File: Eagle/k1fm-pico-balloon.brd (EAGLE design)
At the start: 26.4 x 41.1 mm, 42 parts, among them J1 I2C, J2 ICSP, J3 SERIAL, J4 POWER, Q1 ASTX-H11-25.000MHZ-T, Q2 DMP2305U, Q3 DMP2305U, U1 ATMEGA328, U2 Si5351A-B-GT, U3 MCP1754X-XXXXX/C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

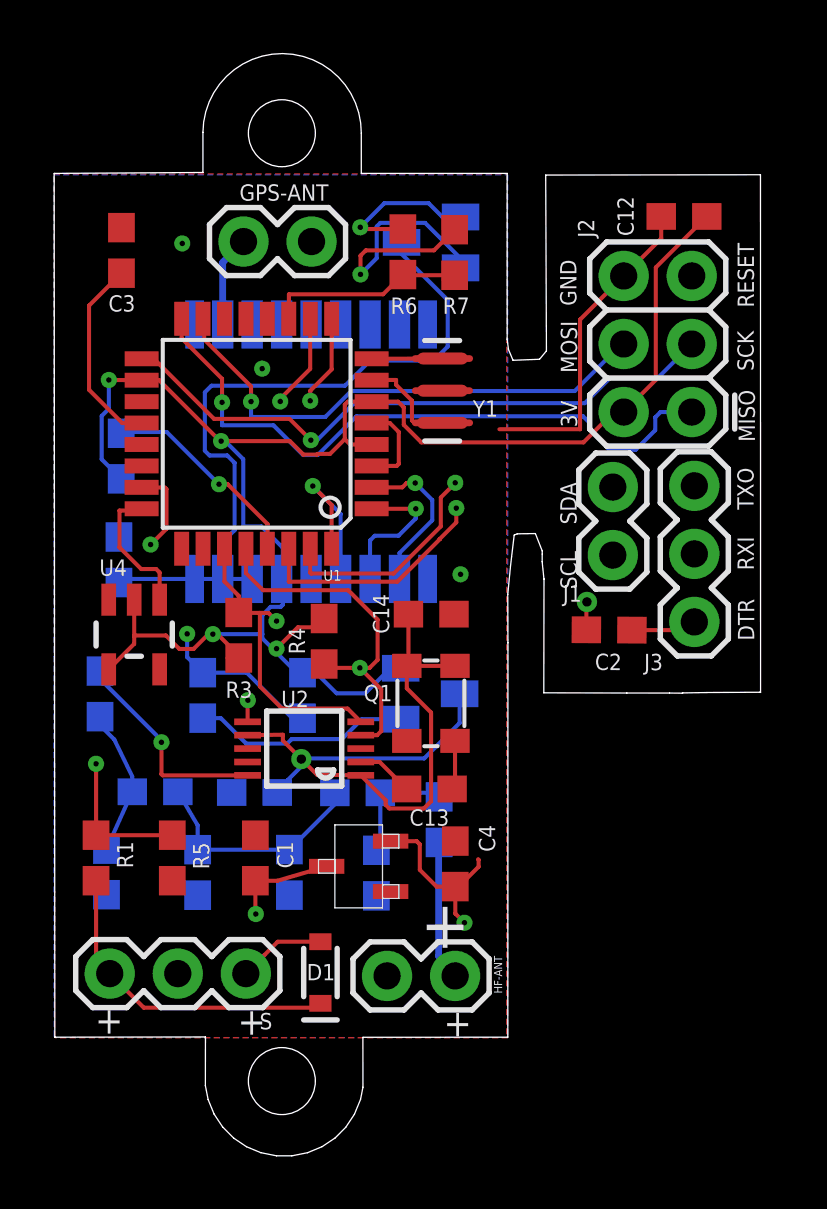
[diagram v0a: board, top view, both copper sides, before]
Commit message: Fix Mosfet polarization
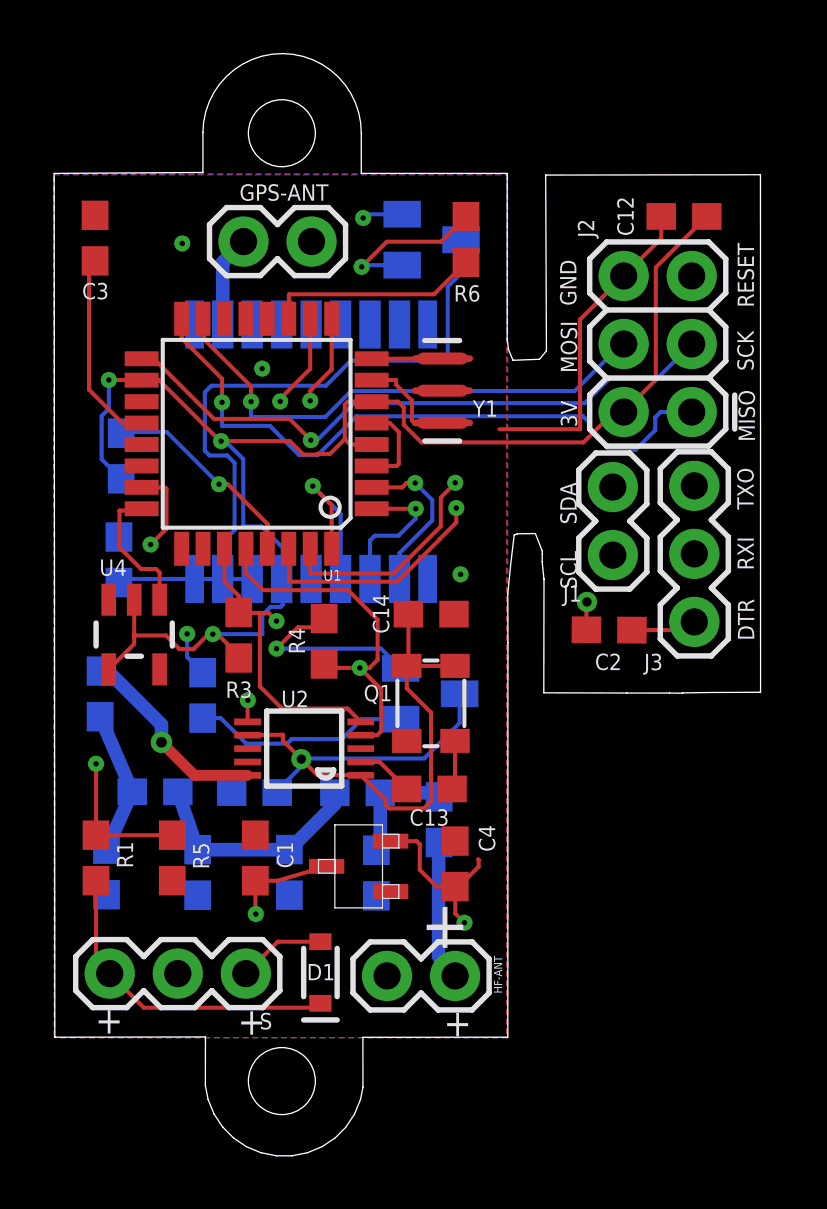
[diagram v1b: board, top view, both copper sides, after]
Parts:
- removed R7, R9: 10k, SparkFun-Resistors:0603
- R6, R8: value 150 -> 1K
- moved R6 2.40 mm to (14.4, 77.5)
- moved C3 1.09 mm to (0.53, 77.6)
- moved Q2 0.10 mm to (13.1, 77.5), turned to 90 degrees
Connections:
- net 3V: no longer R7.2, R9.2
- net GPS_E: no longer R7.1
- net TX_E: no longer R9.1
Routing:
- net 3V: track 110.6 -> 101.7 mm
- net TX_E: track 20.0 -> 15.6 mm
- net GPS_E: track 7.42 -> 8.06 mm
- net N$5: track 5.94 -> 6.49 mm
- net CLK0: track 8.03 -> 7.51 mm
- net N$12: track 6.36 -> 5.84 mm

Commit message: Expand gap
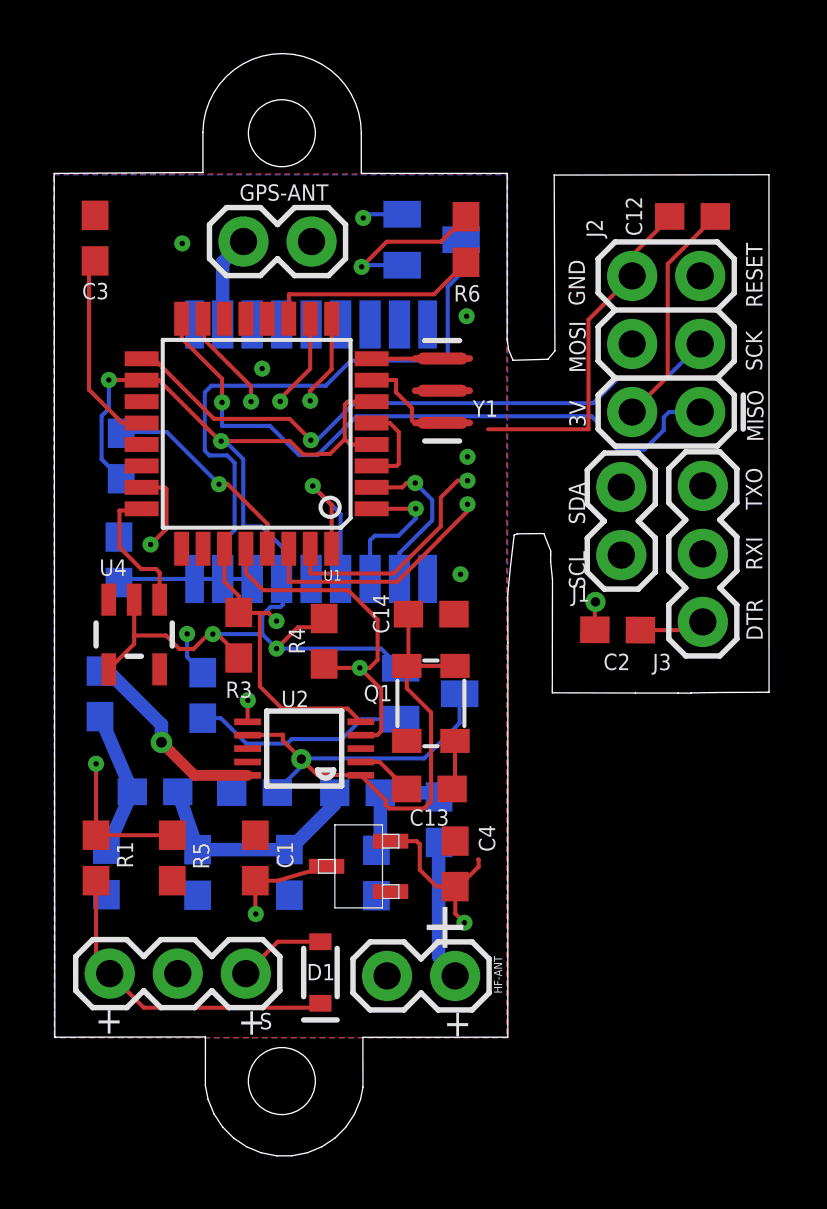
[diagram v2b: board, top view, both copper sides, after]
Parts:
- moved C12 0.32 mm to (22.8, 78.4)
- moved J2 0.32 mm to (23.1, 71.1)
- moved J3 0.32 mm to (23.2, 63.3)
- moved C2 0.32 mm to (20.0, 63.0)
- moved J1 0.32 mm to (20.2, 68.3)
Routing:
- net 3V: track 101.7 -> 108.0 mm
- net GND: track 15.6 -> 16.3 mm, vias 3 -> 5
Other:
- board size 26.4 x 41.1 mm -> 26.7 x 41.1 mm

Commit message: Fixed R1-R5 voltage divider, fixed PCB warnings
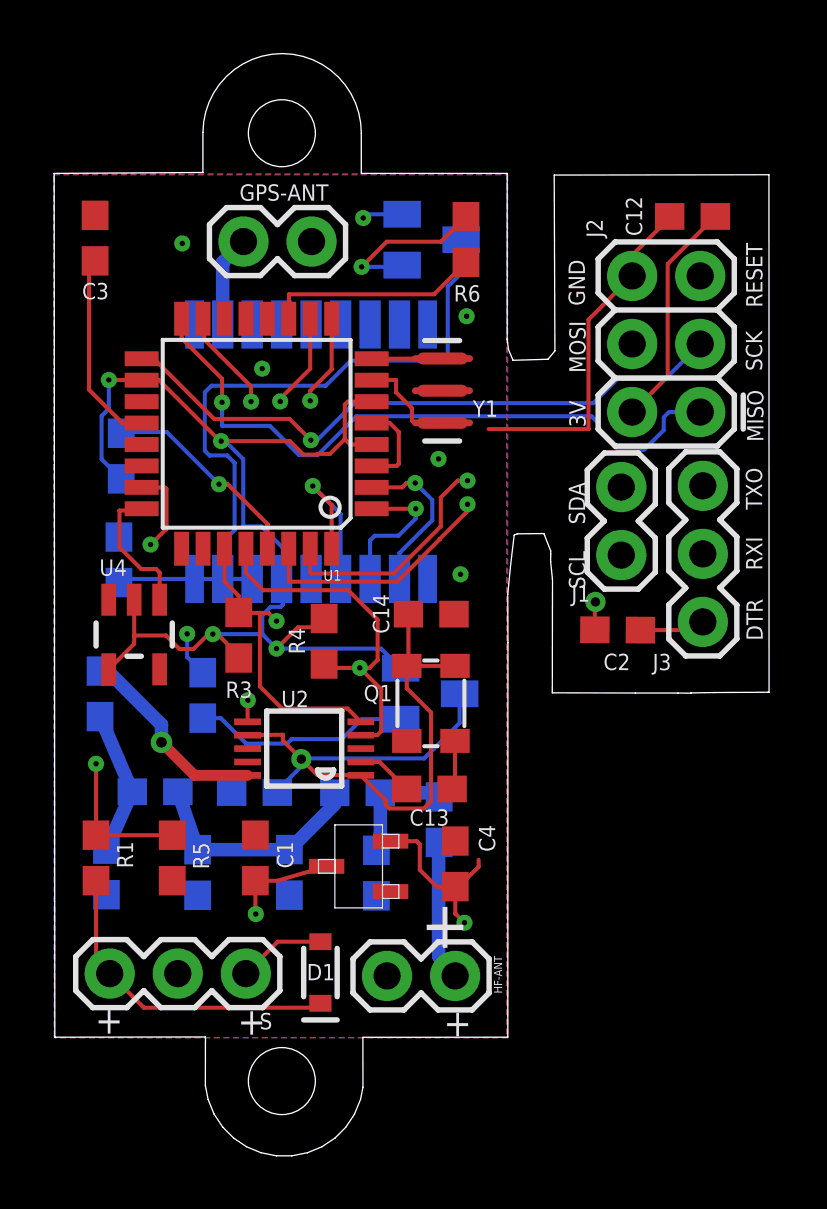
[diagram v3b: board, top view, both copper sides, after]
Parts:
- R5: value 4.7k -> 1k
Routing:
- net 3V: track 108.0 -> 106.5 mm
- net N$3: track 4.25 -> 3.28 mm
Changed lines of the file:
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@@
 <attribute name="VALUE" x="1.32644375" y="54.44650625" size="0.6096" layer="27" font="vector" ratio="20" rot="R90" align="top-center"/>
 </element>
-<element name="R5" library="SparkFun-Resistors" library_urn="urn:adsk.eagle:library:532" package="0603" package3d_urn="urn:adsk.eagle:package:39650/1" value="4.7k" x="3.40955" y="54.446978125" smashed="yes" rot="R90">
+<element name="R5" library="SparkFun-Resistors" library_urn="urn:adsk.eagle:library:532" package="0603" package3d_urn="urn:adsk.eagle:package:39650/1" value="1k" x="3.40955" y="54.446978125" smashed="yes" rot="R90">
 <attribute name="NAME" x="4.78984375" y="54.52568125" size="0.6096" layer="25" font="vector" ratio="20" rot="R90" align="bottom-center"/>
 <attribute name="PROD_ID" value="RES-00824" x="3.40955" y="54.446978125" size="1.27" layer="27" rot="R90" display="off"/>
@@
 <wire x1="20.5768875" y1="76.942765625" x2="20.5768875" y2="76.1720125" width="0.1524" layer="1"/>
 <wire x1="20.5768875" y1="76.1720125" x2="18.947928125" y2="74.543053125" width="0.1524" layer="1"/>
-<wire x1="18.947928125" y1="74.543053125" x2="18.947928125" y2="70.44936875" width="0.1524" layer="1"/>
+<wire x1="18.947928125" y1="74.543053125" x2="18.947928125" y2="70.45523125" width="0.1524" layer="1"/>
 <wire x1="10.850665625" y1="70.68035625" x2="11.53163125" y2="70.68035625" width="0.1524" layer="1"/>
 <wire x1="11.53163125" y1="70.68035625" x2="11.86534375" y2="70.34664375" width="0.1524" layer="1"/>
@@
 <via x="3.781075" y="77.385203125" extent="1-16" drill="0.2"/>
 <via x="14.3971125" y="74.66815" extent="1-16" drill="0.2"/>
-<via x="14.429625" y="69.4192" extent="1-16" drill="0.2"/>
-<wire x1="18.947928125" y1="70.44936875" x2="15.198228125" y2="70.44936875" width="0.1524" layer="1"/>
+<via x="13.348934375" y="69.3406125" extent="1-16" drill="0.2"/>
+<wire x1="18.947928125" y1="70.45523125" x2="15.21810625" y2="70.45523125" width="0.1524" layer="1"/>
 </signal>
 <signal name="3V">
@@
 <contactref element="U4" pad="4"/>
 <contactref element="GPS1" pad="6_V_BCKP"/>
-<wire x1="1.036578125" y1="61.486290625" x2="1.095696875" y2="61.486290625" width="0.1524" layer="1"/>
 <wire x1="1.98658125" y1="64.0864875" x2="1.986578125" y2="64.086490625" width="0.1524" layer="1"/>
-<wire x1="1.036578125" y1="61.358659375" x2="1.036578125" y2="61.486290625" width="0.1524" layer="1"/>
-<wire x1="7.379503125" y1="64.749571875" x2="7.49139375" y2="64.8614625" width="0.1524" layer="16"/>
 <contactref element="Q3" pad="2"/>
 <wire x1="2.265465625" y1="72.28035625" x2="1.041303125" y2="72.288534375" width="0.1524" layer="1"/>
 <via x="1.041303125" y="72.288534375" extent="1-16" drill="0.2"/>
-<wire x1="11.538078125" y1="55.050225" x2="11.56031875" y2="55.072465625" width="0.1524" layer="1"/>
 <contactref element="Q2" pad="2"/>
 <via x="10.53673125" y="78.335784375" extent="1-16" drill="0.2"/>
@@
 <wire x1="14.3156125" y1="52.028271875" x2="9.806440625" y2="56.53744375" width="0.1524" layer="2"/>
 <wire x1="9.806440625" y1="56.53744375" x2="7.428621875" y2="56.53744375" width="0.1524" layer="2"/>
-<wire x1="14.824553125" y1="54.3973375" x2="14.843965625" y2="54.377925" width="0.1524" layer="1"/>
 <wire x1="14.843965625" y1="54.377925" x2="14.843965625" y2="54.11790625" width="0.1524" layer="1"/>
 <wire x1="14.843965625" y1="54.11790625" x2="14.1030125" y2="53.376953125" width="0.1524" layer="1"/>
@@
 <via x="7.30088125" y="62.26031875" extent="1-16" drill="0.2"/>
 <wire x1="8.7500375" y1="63.05695625" x2="8.09751875" y2="63.05695625" width="0.1524" layer="1"/>
-<wire x1="5.890165625" y1="61.910128125" x2="5.4615625" y2="61.910128125" width="0.1524" layer="1"/>
 <wire x1="1.036578125" y1="61.486290625" x2="1.98658125" y2="62.43629375" width="0.1524" layer="1"/>
 <wire x1="1.98658125" y1="62.43629375" x2="1.98658125" y2="62.73780625" width="0.1524" layer="1"/>
@@
 <wire x1="3.6738125" y1="62.247834375" x2="3.1702125" y2="62.751434375" width="0.1524" layer="1"/>
 <wire x1="4.92489375" y1="62.801778125" x2="4.92489375" y2="59.041171875" width="0.1524" layer="2"/>
-<wire x1="4.92489375" y1="62.801778125" x2="4.72475625" y2="62.801778125" width="0.1524" layer="16"/>
 <wire x1="5.23128125" y1="70.006771875" x2="7.798621875" y2="70.006771875" width="0.1524" layer="1"/>
 <wire x1="8.81243125" y1="69.50388125" x2="8.837928125" y2="69.529378125" width="0.1524" layer="1"/>
@@
 <wire x1="0.7723875" y1="69.32840625" x2="0.7723875" y2="70.94449375" width="0.1524" layer="16"/>
 <wire x1="1.5009875" y1="68.59980625" x2="0.7723875" y2="69.32840625" width="0.1524" layer="16"/>
-<wire x1="11.9356375" y1="61.52650625" x2="11.37726875" y2="61.52650625" width="0.1524" layer="16"/>
 <wire x1="7.30088125" y1="62.26031875" x2="11.201825" y2="62.26031875" width="0.1524" layer="16"/>
 <wire x1="11.201825" y1="62.26031875" x2="11.9356375" y2="61.52650625" width="0.1524" layer="16"/>
@@
 <contactref element="C2" pad="2"/>
 <contactref element="R2" pad="1"/>
-<wire x1="6.958065625" y1="65.98775625" x2="6.97814375" y2="65.967678125" width="0.1524" layer="1"/>
 <contactref element="J2" pad="5"/>
 <wire x1="19.18414375" y1="62.963075" x2="19.18414375" y2="63.9817375" width="0.1524" layer="1"/>
@@
 <contactref element="C6" pad="2"/>
 <contactref element="L1" pad="2"/>
-<wire x1="0.7136" y1="59.721709375" x2="0.399321875" y2="60.0359875" width="0.1524" layer="16"/>
 <wire x1="1.914634375" y1="56.918090625" x2="0.9513875" y2="54.774478125" width="0.508" layer="16"/>
 <wire x1="0.7136" y1="59.721709375" x2="1.914634375" y2="56.918090625" width="0.508" layer="16"/>
@@
 <contactref element="R6" pad="2"/>
 <via x="10.477465625" y="76.510840625" extent="1-16" drill="0.2"/>
-<wire x1="11.705459375" y1="76.575453125" x2="11.989153125" y2="76.575453125" width="0.1524" layer="16"/>
-<wire x1="11.989153125" y1="76.575453125" x2="10.542078125" y2="76.575453125" width="0.1524" layer="16"/>
-<wire x1="10.542078125" y1="76.575453125" x2="10.477465625" y2="76.510840625" width="0.1524" layer="16"/>
 <wire x1="10.477465625" y1="76.510840625" x2="11.4164375" y2="77.4498125" width="0.1524" layer="1"/>
 <wire x1="13.4407125" y1="77.4498125" x2="14.37328125" y2="78.38238125" width="0.1524" layer="1"/>
 <wire x1="11.4164375" y1="77.4498125" x2="13.4407125" y2="77.4498125" width="0.1524" layer="1"/>
+<wire x1="10.477465625" y1="76.510840625" x2="11.924540625" y2="76.510840625" width="0.1524" layer="16"/>
+<wire x1="11.924540625" y1="76.510840625" x2="11.989153125" y2="76.575453125" width="0.1524" layer="16"/>
 </signal>
 <signal name="GPS_E">
 <contactref element="R6" pad="1"/>
-<wire x1="14.37328125" y1="76.68238125" x2="14.399290625" y2="76.656371875" width="0.1524" layer="1"/>
 <contactref element="U1" pad="11"/>
 <wire x1="7.758065625" y1="74.57295625" x2="7.763240625" y2="74.57813125" width="0.1524" layer="1"/>
@@
 <contactref element="U1" pad="10"/>
 <contactref element="R8" pad="1"/>
-<wire x1="8.558065625" y1="74.57295625" x2="8.720771875" y2="74.41025" width="0.1524" layer="1"/>
 <via x="3.9646125" y="62.809840625" extent="1-16" drill="0.2"/>
 <wire x1="4.545071875" y1="61.363275" x2="3.9646125" y2="61.943734375" width="0.1524" layer="16"/>
@@
 <wire x1="7.4379" y1="71.48775625" x2="7.438146875" y2="70.55664375" width="0.1524" layer="2"/>
 <wire x1="7.438146875" y1="70.55664375" x2="6.97175625" y2="70.090253125" width="0.1524" layer="2"/>
-<wire x1="3.9646125" y1="64.54423125" x2="3.9646125" y2="62.809840625" width="0.1524" layer="2"/>
-<wire x1="6.97175625" y1="70.090253125" x2="6.97175625" y2="67.551375" width="0.1524" layer="2"/>
-<wire x1="6.97175625" y1="67.551375" x2="3.9646125" y2="64.54423125" width="0.1524" layer="2"/>
+<wire x1="3.9646125" y1="62.809840625" x2="3.9646125" y2="64.54423125" width="0.1524" layer="2"/>
+<wire x1="6.97175625" y1="67.551375" x2="6.97175625" y2="70.090253125" width="0.1524" layer="2"/>
+<wire x1="3.9646125" y1="64.54423125" x2="6.97175625" y2="67.551375" width="0.1524" layer="2"/>
 </signal>
 <signal name="N$15">
@@
 <contactref element="Q2" pad="3"/>
 <wire x1="6.39139375" y1="64.8614625" x2="5.29139375" y2="64.8614625" width="0.1524" layer="16"/>
-<wire x1="5.29139375" y1="64.8614625" x2="4.30098125" y2="64.8614625" width="0.1524" layer="16"/>
-<wire x1="4.30098125" y1="64.8614625" x2="4.24139375" y2="64.8614625" width="0.1524" layer="16"/>
+<wire x1="5.29139375" y1="64.8614625" x2="4.24139375" y2="64.8614625" width="0.1524" layer="16"/>
 <wire x1="13.65965" y1="73.01114375" x2="13.69059375" y2="73.0420875" width="0.1524" layer="16"/>
 <contactref element="C10" pad="1"/>
-<wire x1="4.1656" y1="64.72608125" x2="4.30098125" y2="64.8614625" width="0.1524" layer="16"/>
 <wire x1="5.7354625" y1="66.68179375" x2="5.7354625" y2="69.1957375" width="0.1524" layer="16"/>
 <wire x1="5.7354625" y1="66.68179375" x2="5.287234375" y2="66.233565625" width="0.1524" layer="16"/>
@@
 <signal name="N$3">
 <contactref element="J4" pad="3"/>
-<wire x1="6.154065625" y1="50.128775" x2="6.84034375" y2="50.815053125" width="0.1524" layer="1"/>
 <contactref element="D1" pad="A"/>
-<wire x1="6.154065625" y1="50.128775" x2="7.34465" y2="51.319359375" width="0.1524" layer="1"/>
-<wire x1="7.34465" y1="51.319359375" x2="8.938628125" y2="51.319359375" width="0.1524" layer="1"/>
+<wire x1="8.938628125" y1="51.319359375" x2="7.34465" y2="51.319359375" width="0.1524" layer="1"/>
+<wire x1="7.34465" y1="51.319359375" x2="6.154065625" y2="50.128775" width="0.1524" layer="1"/>
 </signal>
 <signal name="RXI">
@@
 <wire x1="0.56444375" y1="57.959628125" x2="0.56304375" y2="57.961028125" width="0.1524" layer="1"/>
 <via x="0.56304375" y="57.961028125" extent="1-16" drill="0.2"/>
-<wire x1="2.316628125" y1="68.22919375" x2="2.265465625" y2="68.28035625" width="0.1524" layer="1"/>
 <wire x1="2.265465625" y1="68.28035625" x2="2.27230625" y2="68.273515625" width="0.1524" layer="1"/>
 <wire x1="2.27230625" y1="68.273515625" x2="3.13168125" y2="68.273515625" width="0.1524" layer="1"/>
